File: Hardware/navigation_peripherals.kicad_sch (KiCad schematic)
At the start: 5 parts, among them U10 NEO-M8N-0, U11 BMP390, U12 IST8310, U8 24CW1280T-I/OT, U9 BMI088

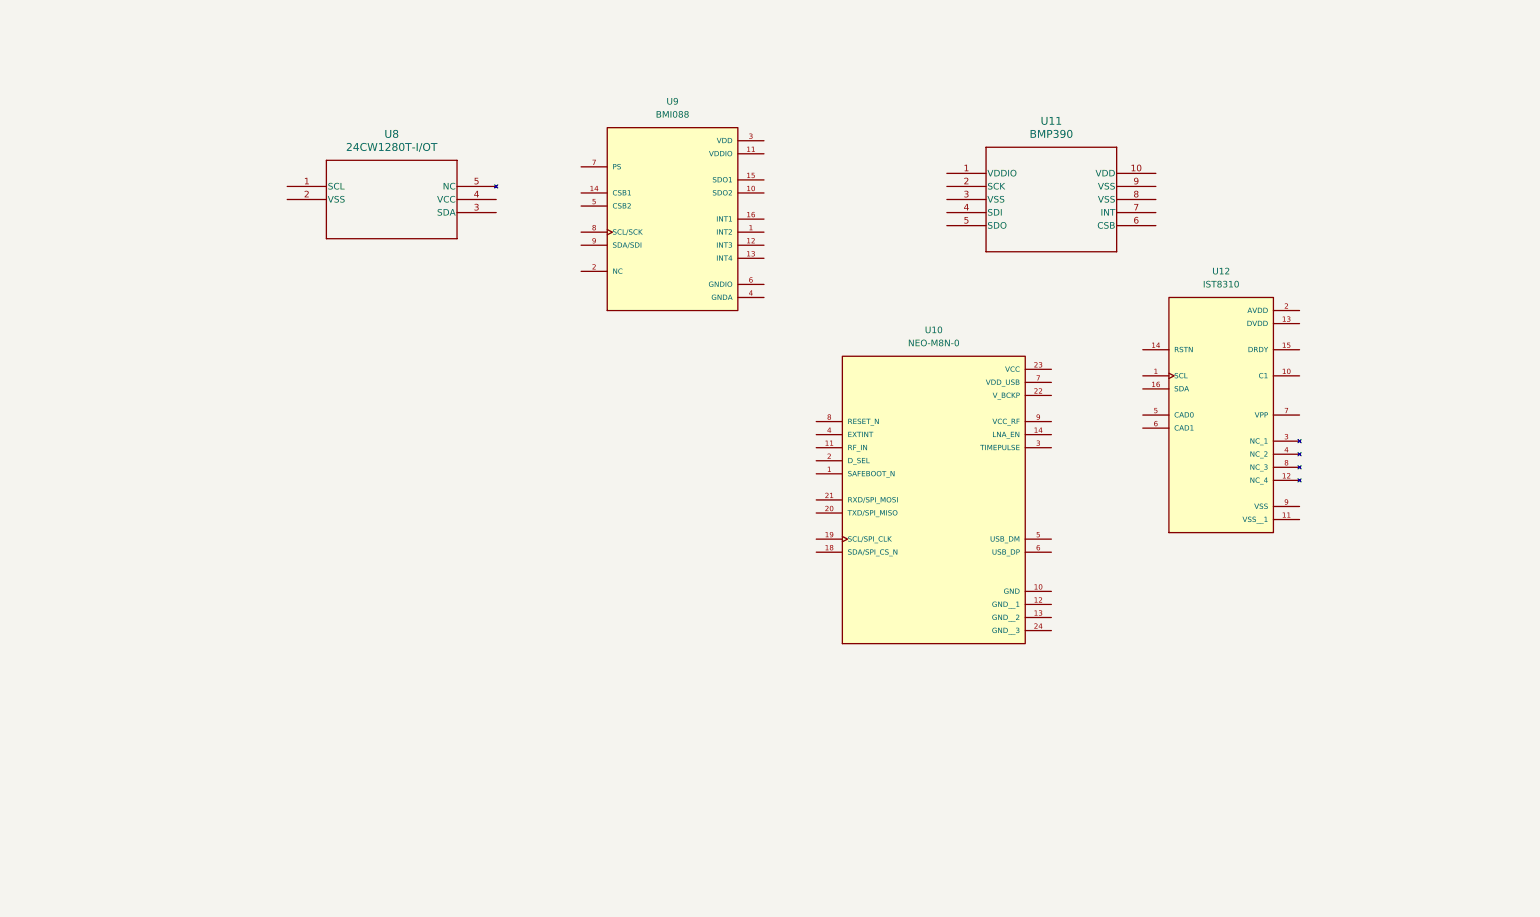
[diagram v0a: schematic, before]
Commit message: fcu, nu schematics, problem with pins
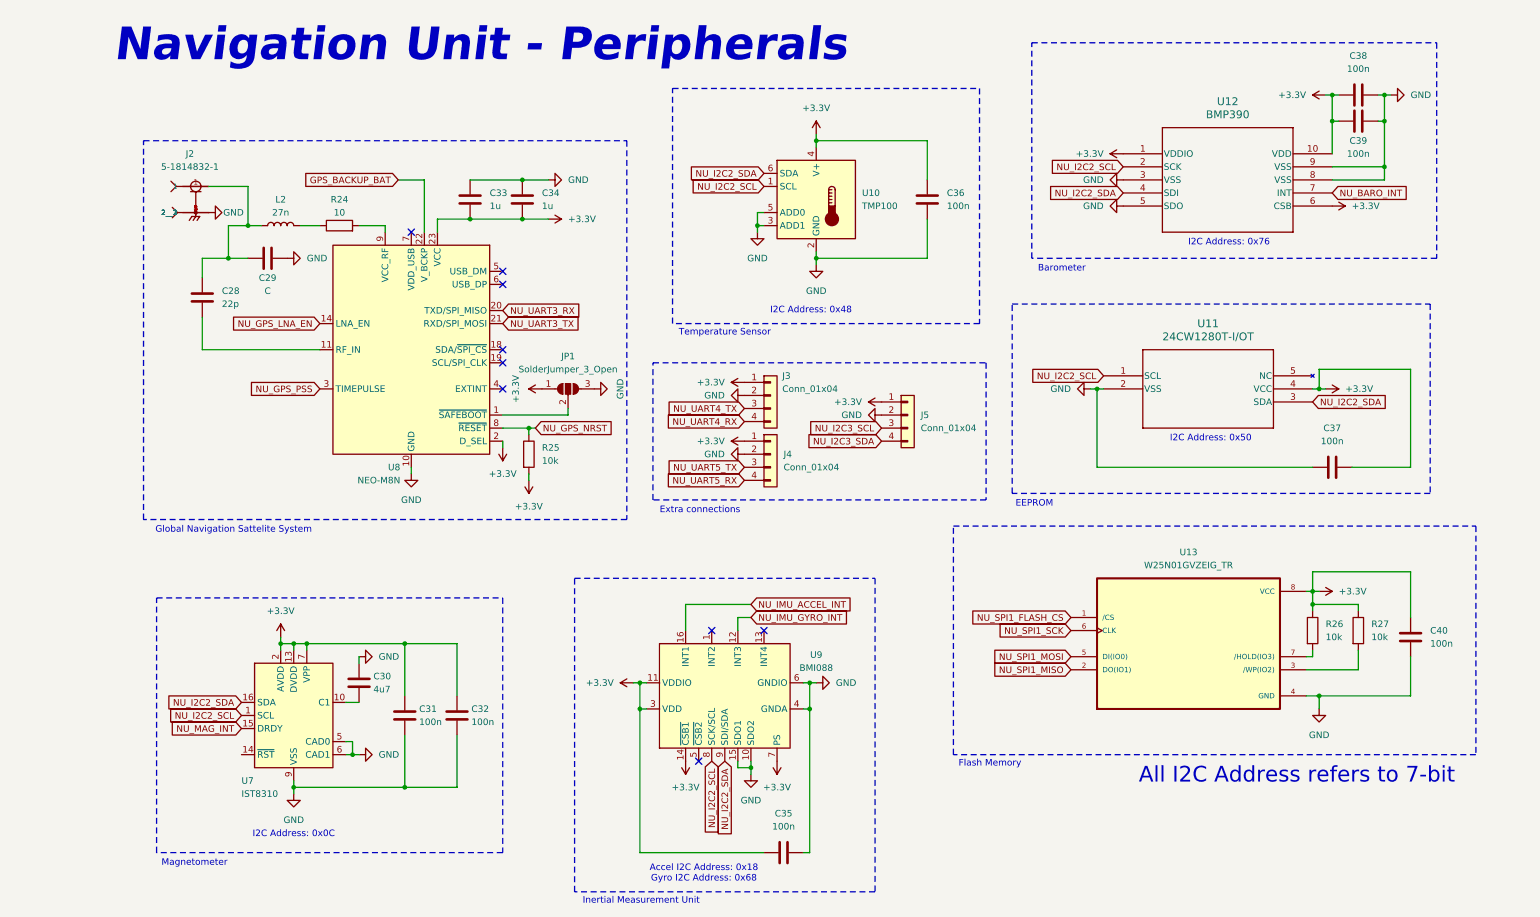
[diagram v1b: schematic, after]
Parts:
- removed U10: NEO-M8N-0, NEO-M8N-0:XCVR_NEO-M8N-0, symbol Aircraft_Components:NEO-M8N-0
- removed U12: IST8310, IST8310:PQFN50P300X300X110-16N, symbol Aircraft_Components:IST8310
- removed U8: 24CW1280T-I/OT, SOT-23-5_2P9X1P6_MCH, symbol Aircraft_Components:24CW1280T-I_OT
- removed U9: BMI088, BMI088:PQFN50P450X300X100-16N, symbol Aircraft_Components:BMI088
- added C28: 22p, symbol Device:C
- added C29: C, symbol Device:C
- added C30: 4u7, symbol Device:C
- added C31, C32, C35, C36, C37, C38, C39, C40: 100n, symbol Device:C
- added C33, C34: 1u, symbol Device:C
- added J2: 5-1814832-1, 5-1814832-1:TE_5-1814832-1, symbol Aircraft_Components:5-1814832-1
- added J3, J4, J5: Conn_01x04, symbol Connector_Generic:Conn_01x04
- added JP1: SolderJumper_3_Open, symbol Jumper:SolderJumper_3_Open
- added L2: 27n, symbol Device:L
- added R24: 10, symbol Device:R
- added R25, R26, R27: 10k, symbol Device:R
- added U10: TMP100, Package_TO_SOT_SMD:SOT-23-6, symbol Sensor_Temperature:TMP100
- added U11: 24CW1280T-I/OT, SOT-23-5_2P9X1P6_MCH, symbol Aircraft_Components:24CW1280T-I_OT
- added U13: W25N01GVZEIG_TR, W25N01GVZEIG_TR:SON127P800X600X80-9N, symbol Aircraft_Components:W25N01GVZEIG_TR
- added U7: IST8310, Package_LGA:LGA-16_3x3mm_P0.5mm, symbol Sensor_Magnetic:IST8310
- added U8: NEO-M8N, RF_GPS:ublox_NEO, symbol RF_GPS:NEO-M8N
- added U9: BMI088, Package_LGA:Bosch_LGA-16_4.5x3mm_P0.5mm_LayoutBorder7x1y_ClockwisePinNumbering, symbol Sensor_Motion:BMI088
- renumbered U11 to U12
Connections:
- net +3.3V: now reaches U12.1 (VDDIO)
- net +3.3V: now also U12.10 (VDD), U12.6 (CSB), C31.1, C32.1, C33.2, C34.2, C35.1, C36.2, C37.1, C38.2, C39.2, C40.1, J3.1 (Pin_1), J4.1 (Pin_1), J5.1 (Pin_1), JP1.1 (A), R25.2, R26.1, R27.1, U10.4 (V+), U11.4 (VCC), U13.8 (VCC), U7.13 (DVDD), U7.2 (AVDD), U7.7 (VPP), U8.2 (D_SEL), U8.23 (VCC), U9.11 (VDDIO), U9.14 (~{CSB1}), U9.3 (VDD), U9.7 (PS)
- net NU_I2C2_SCL: now reaches U12.2 (SCK)
- net NU_I2C2_SCL: now also U10.1 (SCL), U11.1 (SCL), U7.1 (SCL), U9.8 (SCK/SCL)
- net GND: now reaches U12.3 (VSS)
- net GND: now also U12.5 (SDO), U12.8 (VSS), U12.9 (VSS), C29.2, C30.1, C31.2, C32.2, C33.1, C34.1, C35.2, C36.1, C37.2, C38.1, C39.1, C40.2, J2.2, J2.3 (2__1), J2.4 (2__2), J2.5 (2__3), J3.2 (Pin_2), J4.2 (Pin_2), J5.2 (Pin_2), JP1.3 (B), U10.2 (GND), U10.3 (ADD1), U10.5 (ADD0), U11.2 (VSS), U13.4 (GND), U7.11 (VSS), U7.5 (CAD0), U7.6 (CAD1), U7.9 (VSS), U8.10 (GND), U8.12 (GND), U8.13 (GND), U8.24 (GND), U9.10 (SDO2), U9.15 (SDO1), U9.2 (GNDA), U9.4 (GNDA), U9.6 (GNDIO)
- net NU_I2C2_SDA: now reaches U12.4 (SDI)
- net NU_I2C2_SDA: now also U10.6 (SDA), U11.3 (SDA), U7.16 (SDA), U9.9 (SDI/SDA)
- net NU_BARO_INT: now reaches U12.7 (INT)
- new net: C30.2, U7.10 (C1)
- new net: JP1.2 (C), U8.1 (~{SAFEBOOT})
- new net: R26.2, U13.7 (/HOLD(IO3))
- new net: C28.1, C29.1, J2.1, L2.1
- new net: L2.2, R24.1
- new net: R24.2, U8.9 (VCC_RF)
- new net: R27.2, U13.3 (/WP(IO2))
- new net: C28.2, U8.11 (RF_IN)
- new net GPS_BACKUP_BAT: U8.22 (V_BCKP)
- new net NU_GPS_LNA_EN: U8.14 (LNA_EN)
- new net NU_GPS_NRST: R25.1, U8.8 (~{RESET})
- new net NU_GPS_PSS: U8.3 (TIMEPULSE)
- new net NU_I2C3_SCL: J5.3 (Pin_3)
- new net NU_I2C3_SDA: J5.4 (Pin_4)
- new net NU_IMU_ACCEL_INT: U9.16 (INT1)
- new net NU_IMU_GYRO_INT: U9.12 (INT3)
- new net NU_MAG_INT: U7.15 (DRDY)
- new net NU_SPI1_FLASH_CS: U13.1 (/CS)
- new net NU_SPI1_MISO: U13.2 (DO(IO1))
- new net NU_SPI1_MOSI: U13.5 (DI(IO0))
- new net NU_SPI1_SCK: U13.6 (CLK)
- new net NU_UART3_RX: U8.20 (TXD/SPI_MISO)
- new net NU_UART3_TX: U8.21 (RXD/SPI_MOSI)
- new net NU_UART4_RX: J3.4 (Pin_4)
- new net NU_UART4_TX: J3.3 (Pin_3)
- new net NU_UART5_RX: J4.4 (Pin_4)
- new net NU_UART5_TX: J4.3 (Pin_3)
- no-connect marks 0 -> 9
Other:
- note added: "Accel I2C Address: 0x18 Gyro I2C Address: 0x68"
- note added: "All I2C Address refers to 7-bit"
- note added: "Barometer"
- note added: "EEPROM"
- note added: "Extra connections"
- note added: "Flash Memory"
- note added: "Global Navigation Sattelite System"
- note added: "I2C Address: 0x0C"
- note added: "I2C Address: 0x48"
- note added: "I2C Address: 0x50"
- note added: "I2C Address: 0x76"
- note added: "Inertial Measurement Unit"
- note added: "Magnetometer"
- note added: "Navigation Unit - Peripherals"
- note added: "Temperature Sensor"
- company: (none) -> Breno Soares Alves
- title: (none) -> Navigation Unit - Peripherals
- moved on the sheet: U12

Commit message: added projects, schematic almost done, need revision
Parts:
- renumbered C28 to C12, C29 to C13, C30 to C14, C31 to C15, C32 to C16, C33 to C17, C34 to C18, C35 to C19, C36 to C20, C37 to C21, C38 to C22, C39 to C23, C40 to C24, R25 to R10, R26 to R11, R27 to R12, R24 to R9, U12 to U10, U13 to U11, U7 to U5, U8 to U6, U9 to U7, U10 to U8, U11 to U9

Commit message: version 0.1.0
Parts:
- renumbered C12 to C27, C13 to C28, C14 to C29, C15 to C30, C16 to C31, C17 to C32, C18 to C33, C19 to C34, C20 to C35, C21 to C36, C22 to C37, C23 to C38, C24 to C39, R9 to R21, R10 to R22, R11 to R23, R12 to R24
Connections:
- net +3.3V: now also U5.14 (~{RST})
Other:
- note added: "Need Review!!! Just to make sure"
